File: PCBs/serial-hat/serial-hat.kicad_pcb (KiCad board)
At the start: 2 copper layers, 65 x 56 mm, 14 parts, among them CN1 Modem port, CN2 Printer port, J1 Conn_01x02_Pin, J7 Rpi headers, U2 MAX3232

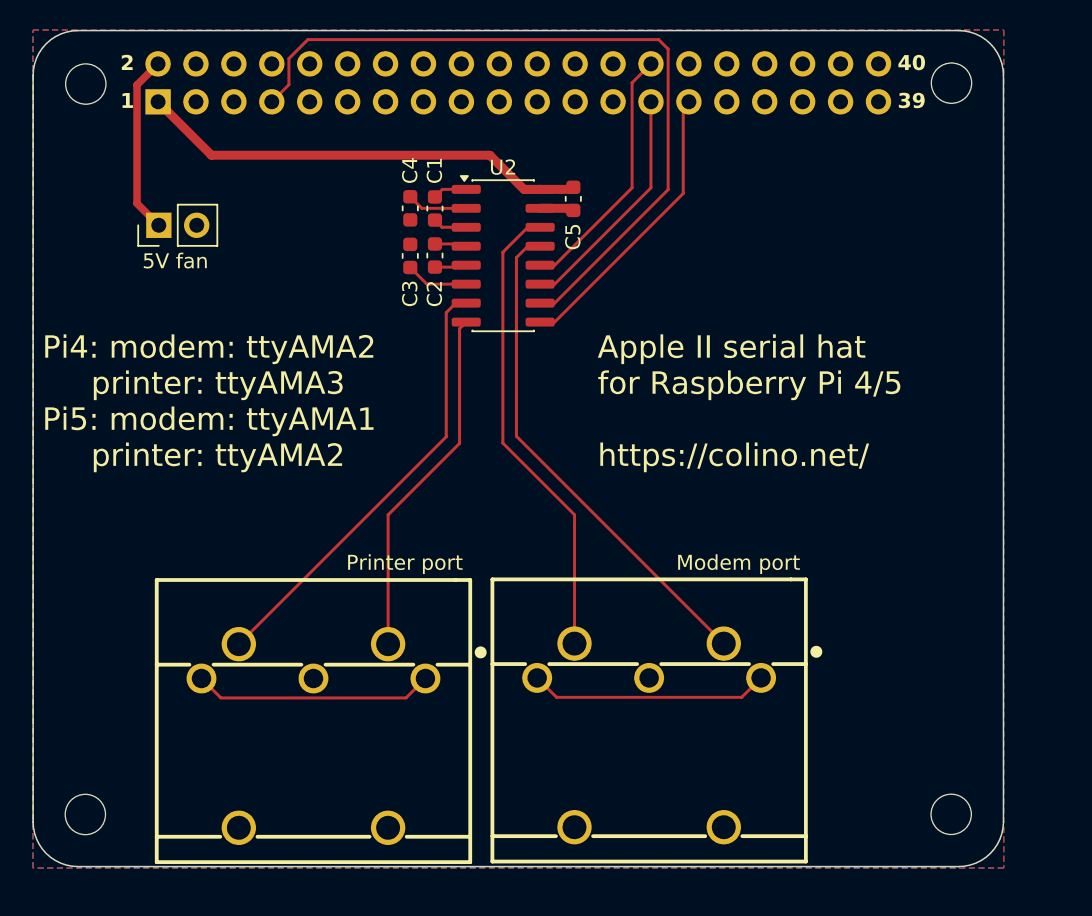
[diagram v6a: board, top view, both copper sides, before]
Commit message: Rework for ventilation hole
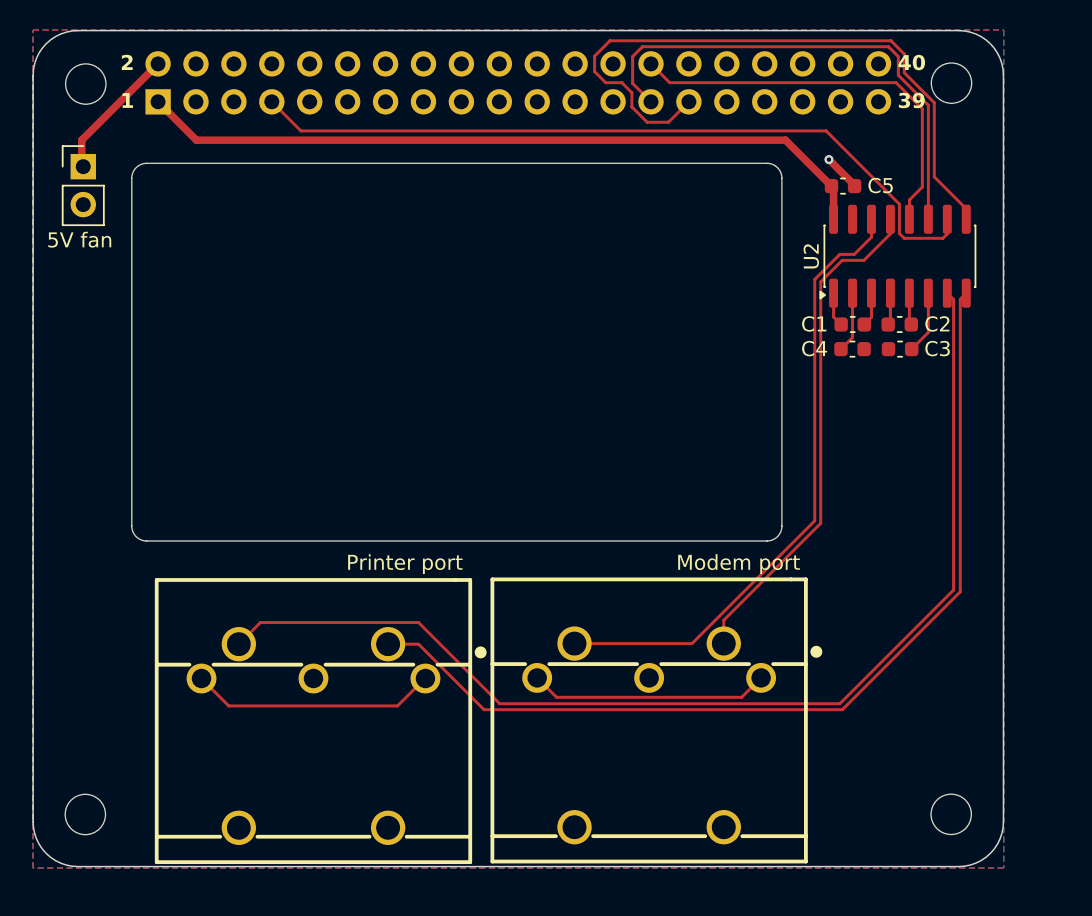
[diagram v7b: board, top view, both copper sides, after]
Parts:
- moved C4 33.4 mm to (180.8, 73.9), turned to 180 degrees
- moved C2 31.5 mm to (180.7, 72.3), turned to 0 degrees
- moved C3 31.1 mm to (177.6, 73.9), turned to 0 degrees
- moved C1 29.0 mm to (177.6, 72.3), turned to 0 degrees
- moved U2 26.6 mm to (180.8, 67.7), turned to 90 degrees
- moved C5 18.1 mm to (176.9, 63.0), turned to 0 degrees
- moved J1 6.40 mm to (126.0, 61.7), turned to 0 degrees
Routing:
- net RX1_in: track 29.6 -> 73.9 mm
- net TX1_in: track 23.7 -> 63.6 mm
- net RX1_OUT_GPIO5: track 19.5 -> 44.2 mm
- net 3.3V: track 30.3 -> 49.7 mm
- net TX0_out_GPIO0: track 15.9 -> 33.6 mm
- net RX0_in: track 31.4 -> 41.8 mm
- net RX0_OUT_GPIO1: track 17.1 -> 27.2 mm
- net 5V: track 12.0 -> 9.04 mm
- net TX1_out_GPIO4: track 50.7 -> 51.3 mm
- net GND: track 2.28 -> 2.49 mm, vias 0 -> 1
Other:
- outline, holes or cut-outs redrawn
- board text added: "Apple II serial hat for Pi 4/5 https://colino.net/"
- board text removed: "Apple II serial hat for Raspberry Pi 4/5 https://colino.net/"

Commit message: Fix CISD Quicktake
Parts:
- moved C4 11.6 mm to (185.6, 63.4), turned to 90 degrees
- moved C5 9.98 mm to (178.7, 72.8)
- moved C3 8.79 mm to (185.6, 70.4), turned to -90 degrees
- moved C2 7.29 mm to (185.6, 66.9), turned to 90 degrees
- moved C1 5.85 mm to (183.4, 72.8), turned to 180 degrees
- moved U2 0.89 mm to (181.0, 66.9), turned to 180 degrees
- moved J1 0.71 mm to (126.5, 62.3)
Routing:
- net RX1_OUT_GPIO5: track 44.2 -> 14.7 mm
- net TX0_out_GPIO0: track 33.6 -> 20.0 mm
- net 3.3V: track 49.7 -> 61.4 mm
- net Net-(U2-C1-): track 2.30 -> 5.39 mm
- net RX0_OUT_GPIO1: track 27.2 -> 25.1 mm
- net Net-(U2-VS+): track 4.07 -> 2.23 mm
- net Net-(U2-VS-): track 4.21 -> 2.41 mm
- net GND: track 2.49 -> 3.93 mm, vias 1 -> 0
- net TX1_in: track 63.6 -> 64.4 mm
- net RX0_in: track 41.8 -> 42.5 mm
- net TX1_out_GPIO4: track 51.3 -> 51.8 mm
- net Net-(U2-C1+): track 2.31 -> 1.78 mm
- net RX1_in: track 73.9 -> 74.5 mm
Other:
- outline, holes or cut-outs redrawn
- board text added: "+5V"
- board text added: "Fan"
- board text added: "GND"
- board text removed: "5V fan"
